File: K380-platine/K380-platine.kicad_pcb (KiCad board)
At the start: 2 copper layers, 98 x 36 mm, 40 parts, among them J1 JST-PH 2, J2 Conn_01x23, J3 MicroMod-M.2E, J4 USB_C_Receptacle_USB2.0, J5 Conn_ARM_JTAG_SWD_10, Q1 PMost Enc FET -20V, Q2 Q_NMOS_DGS, SW1 EG1215AA, SW2 SW_Push, SW3 SW_Push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

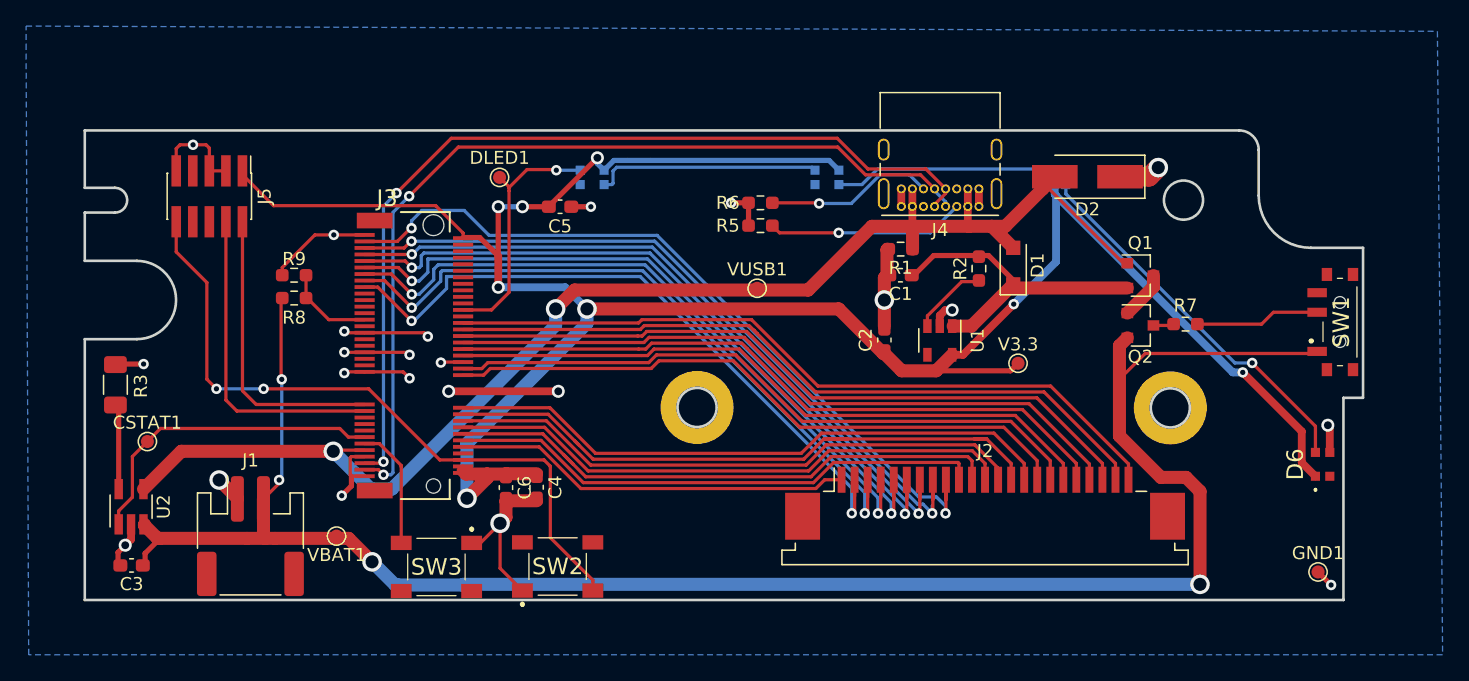
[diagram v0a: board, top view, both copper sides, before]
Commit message: PCB: Fix DRC warnings for PCB
- excluded fix for C4 and C6 from this commit

Signed-off-by: Sophie Tyalie <dev@flowerpot.me>
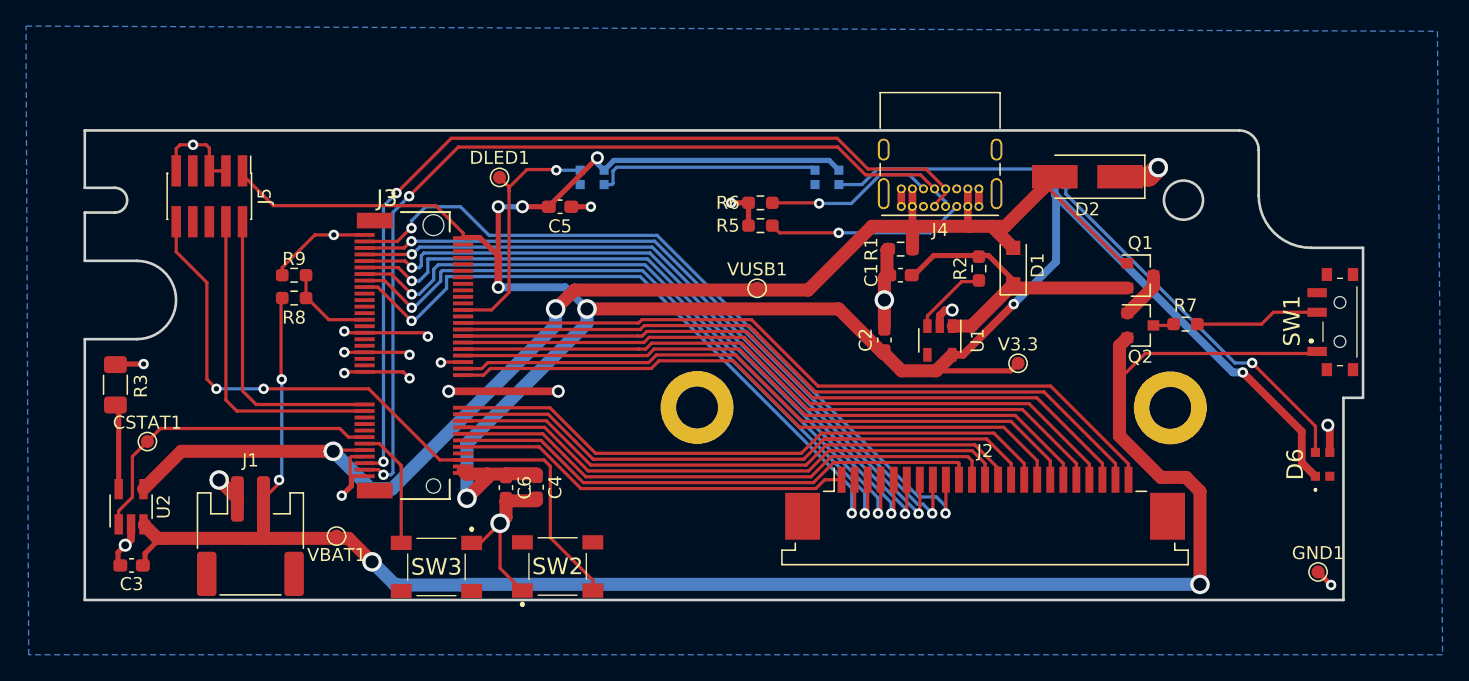
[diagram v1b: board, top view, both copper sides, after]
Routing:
- net ROW7: track 57.1 -> 55.0 mm
- net Net-(C1-Pad1): track 26.0 -> 24.1 mm
- net VBAT: track 144.5 -> 142.8 mm
- net ROW8: track 60.2 -> 58.6 mm
- net ROW5: track 55.3 -> 53.8 mm
- net ROW6: track 55.3 -> 53.8 mm
- net ROW4: track 54.8 -> 53.4 mm
- net ROW3: track 54.1 -> 52.7 mm
- net ROW2: track 53.4 -> 52.1 mm
- net ROW1: track 53.0 -> 51.7 mm
- net COL6: track 49.3 -> 47.9 mm
- net VUSB: track 110.8 -> 109.7 mm
- net COL3: track 43.6 -> 42.6 mm
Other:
- outline, holes or cut-outs redrawn

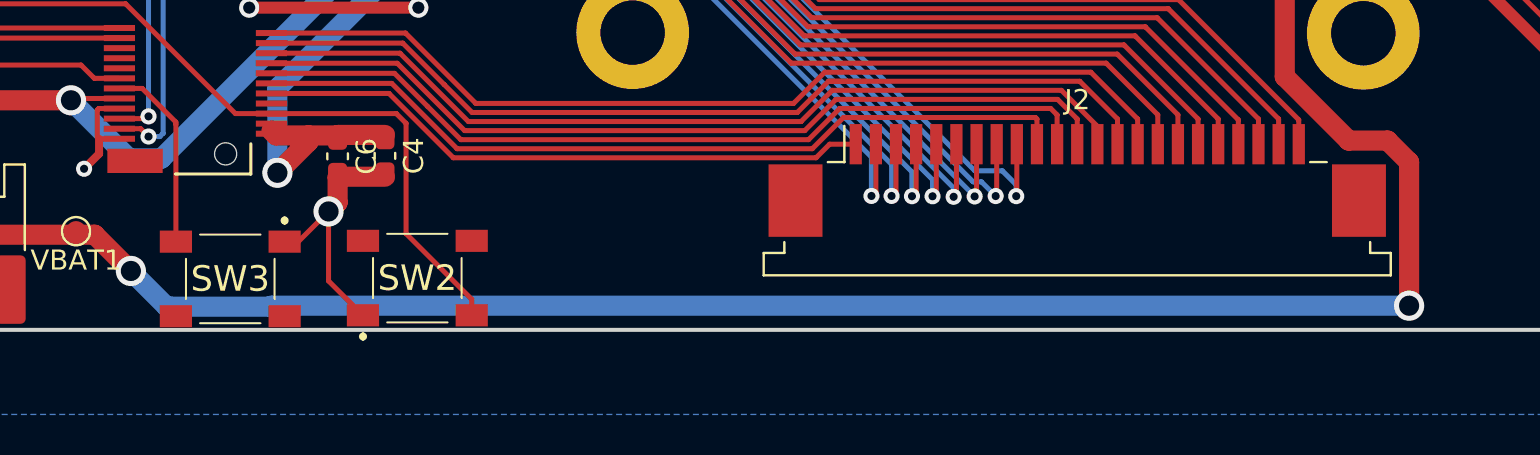
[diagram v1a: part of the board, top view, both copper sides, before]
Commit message: PCB: Fix boot / reset button footprint
The MJTP1140AAUTR is internally differently wired than the original
footprint pad numbers would suggest. This lead to a faulty PCB which
needed a bit of rewiring and trace cutting effort.

Signed-off-by: Sophie Tyalie <dev@flowerpot.me>
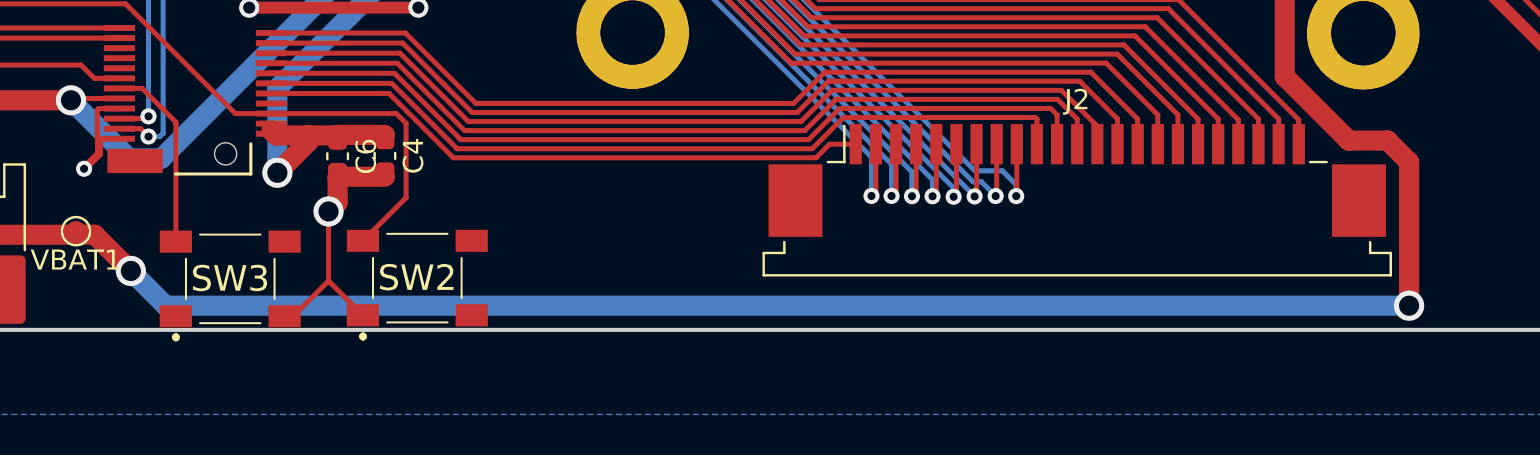
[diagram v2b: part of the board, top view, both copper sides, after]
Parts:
- SW2, SW3: footprint LibraryLoader:MJTP1140AAUTR -> LibraryLoader:MJTP1140AAUTR - Fixed
- turned SW3 to 0 degrees
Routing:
- net RESET: track 53.0 -> 48.9 mm

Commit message: PCB: Moved caps out from under the M.2 module
Due to chosing a M.2 header with a height of 1.8mm instead of 4.2mm, the
space under the SparkFun module decreased significantly. This left no
space for any components under the module, so they needed to be moved.

This affected the 3.3V buffering caps C4 and C6.

Signed-off-by: Sophie Tyalie <dev@flowerpot.me>
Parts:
- moved SW3 12.3 mm to (115.0, 97.8)
- moved SW2 12.3 mm to (124.2, 97.8)
- moved C4 5.19 mm to (106.8, 95.5)
- moved C6 4.77 mm to (105.0, 95.5)
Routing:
- net BOOT: track 9.43 -> 22.6 mm
- net RESET: track 48.9 -> 54.7 mm
- net GND: track 92.6 -> 88.4 mm, vias 23 -> 24
- net V3.3: track 181.4 -> 177.6 mm

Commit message: PCB: Fixed wrongly wired NMOS
I've ordered a GSD mosfet, which didn't go well with the previous
pin layout so needed to change that for further layouts.

Also assigned previously selected footprints to the symbols in the
schematics accordingly (e.g. smaller resistors, …)

Signed-off-by: Sophie Tyalie <dev@flowerpot.me>
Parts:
- R3: footprint Resistor_SMD:R_1206_3216Metric_Pad1.30x1.75mm_HandSolder -> Resistor_SMD:R_0603_1608Metric_Pad0.98x0.95mm_HandSolder
- turned Q2 to 90 degrees
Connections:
- D6 pad 2: Net-(D6-Pad2) -> unconnected-(D6-Pad2)
- J3 pad 15: Net-(J3-Pad15) -> unconnected-(J3-Pad15)
- J3 pad 17: Net-(J3-Pad17) -> unconnected-(J3-Pad17)
- J3 pad 19: Net-(J3-Pad19) -> unconnected-(J3-Pad19)
- J3 pad 47: Net-(J3-Pad47) -> unconnected-(J3-Pad47)
- J3 pad 50: Net-(J3-Pad50) -> unconnected-(J3-Pad50)
- J3 pad 51: Net-(J3-Pad51) -> unconnected-(J3-Pad51)
- J3 pad 53: Net-(J3-Pad53) -> unconnected-(J3-Pad53)
- J3 pad 55: Net-(J3-Pad55) -> unconnected-(J3-Pad55)
- J3 pad 57: Net-(J3-Pad57) -> unconnected-(J3-Pad57)
- J3 pad 60: Net-(J3-Pad60) -> unconnected-(J3-Pad60)
- J3 pad 62: Net-(J3-Pad62) -> unconnected-(J3-Pad62)
- J3 pad 64: Net-(J3-Pad64) -> unconnected-(J3-Pad64)
- J3 pad 66: Net-(J3-Pad66) -> unconnected-(J3-Pad66)
- J3 pad 68: Net-(J3-Pad68) -> unconnected-(J3-Pad68)
- J3 pad 70: Net-(J3-Pad70) -> unconnected-(J3-Pad70)
- J4 pad A8: Net-(J4-PadA8) -> unconnected-(J4-PadA8)
- J4 pad B8: Net-(J4-PadB8) -> unconnected-(J4-PadB8)
- J4 pad S1: Net-(J4-PadS1) -> unconnected-(J4-PadS1)
- J5 pad 6: Net-(J5-Pad6) -> unconnected-(J5-Pad6)
- J5 pad 7: Net-(J5-Pad7) -> unconnected-(J5-Pad7)
- J5 pad 8: Net-(J5-Pad8) -> unconnected-(J5-Pad8)
- Q2 pad 1: Net-(Q1-Pad3) -> Net-(Q2-Pad1)
- Q2 pad 3: Net-(Q2-Pad3) -> Net-(Q1-Pad3)
- R7 pad 1: Net-(Q2-Pad3) -> Net-(Q2-Pad1)
- U1 pad 4: Net-(U1-Pad4) -> unconnected-(U1-Pad4)
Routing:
- net GND: track 88.4 -> 93.5 mm
- net Net-(Q2-Pad1): track 0.00 -> 3.86 mm
- net Net-(Q2-Pad3): track 1.59 -> 0.00 mm
- net VBAT: track 142.7 -> 141.7 mm
